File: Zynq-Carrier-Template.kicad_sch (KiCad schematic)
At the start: 17 parts, among them J1 Zynq_SoM, J2 B2B-PH-K-S, J3 USB_C_Receptacle_USB2.0_16P, J4 Conn_01x03, J5 Conn_01x03, U1 BQ25629RYKR, U12 SRV05-4

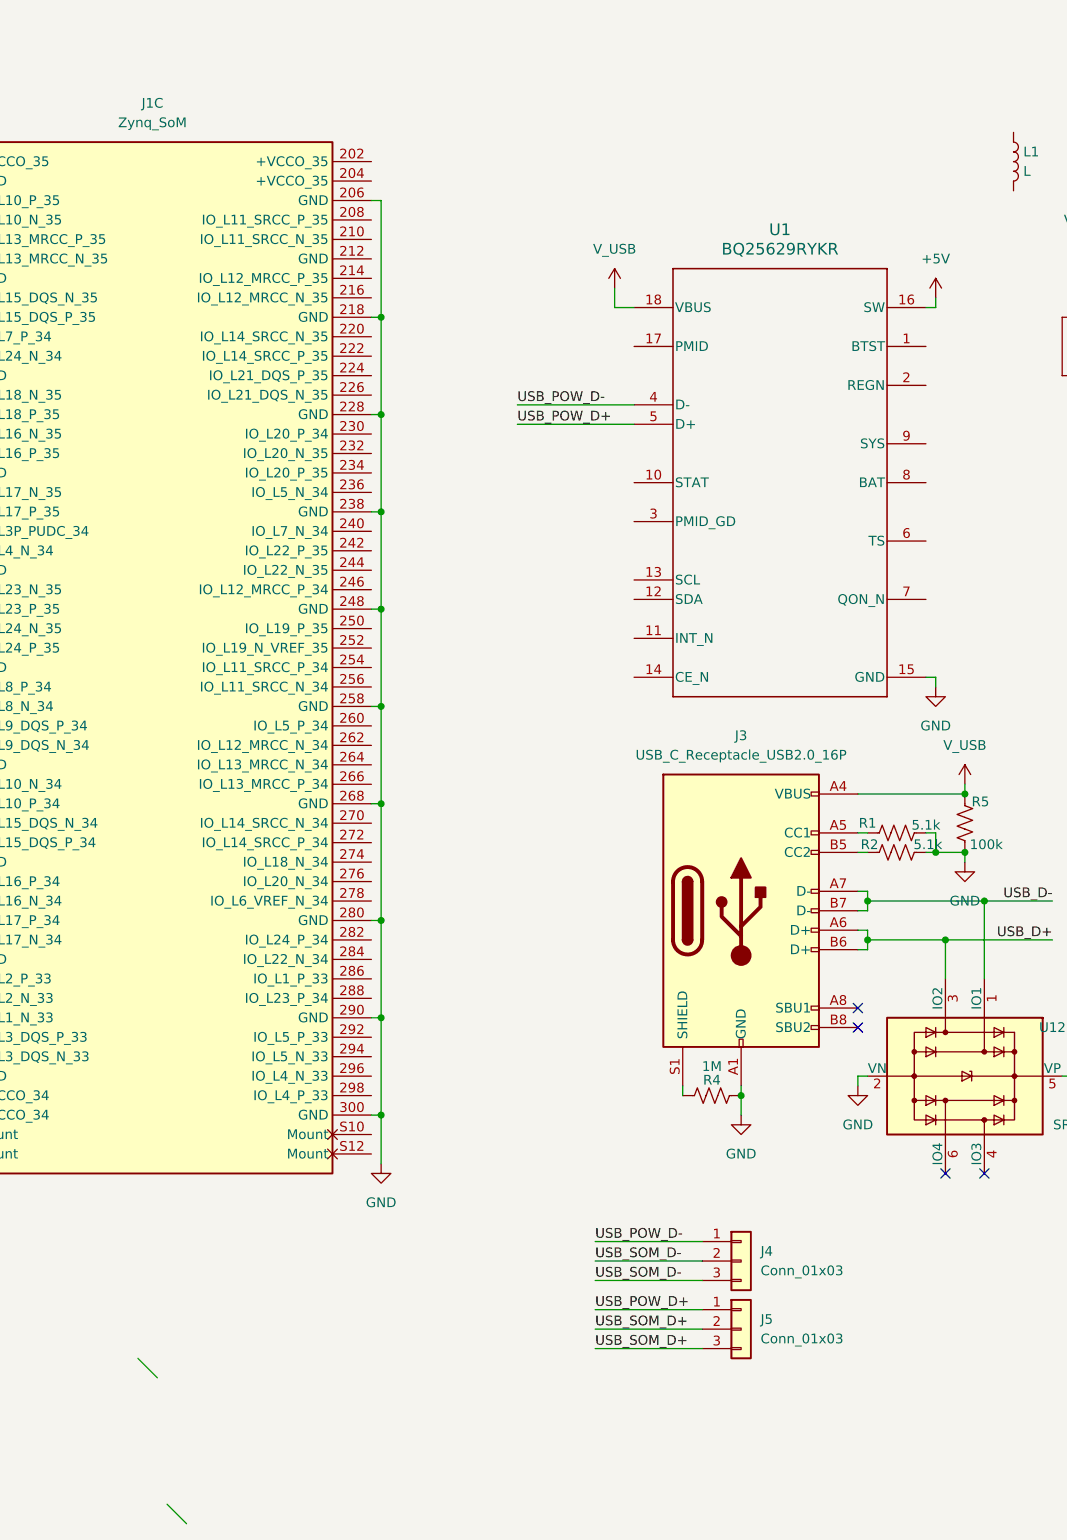
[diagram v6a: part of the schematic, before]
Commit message: Update Zynq-Carrier-Template.kicad_sch
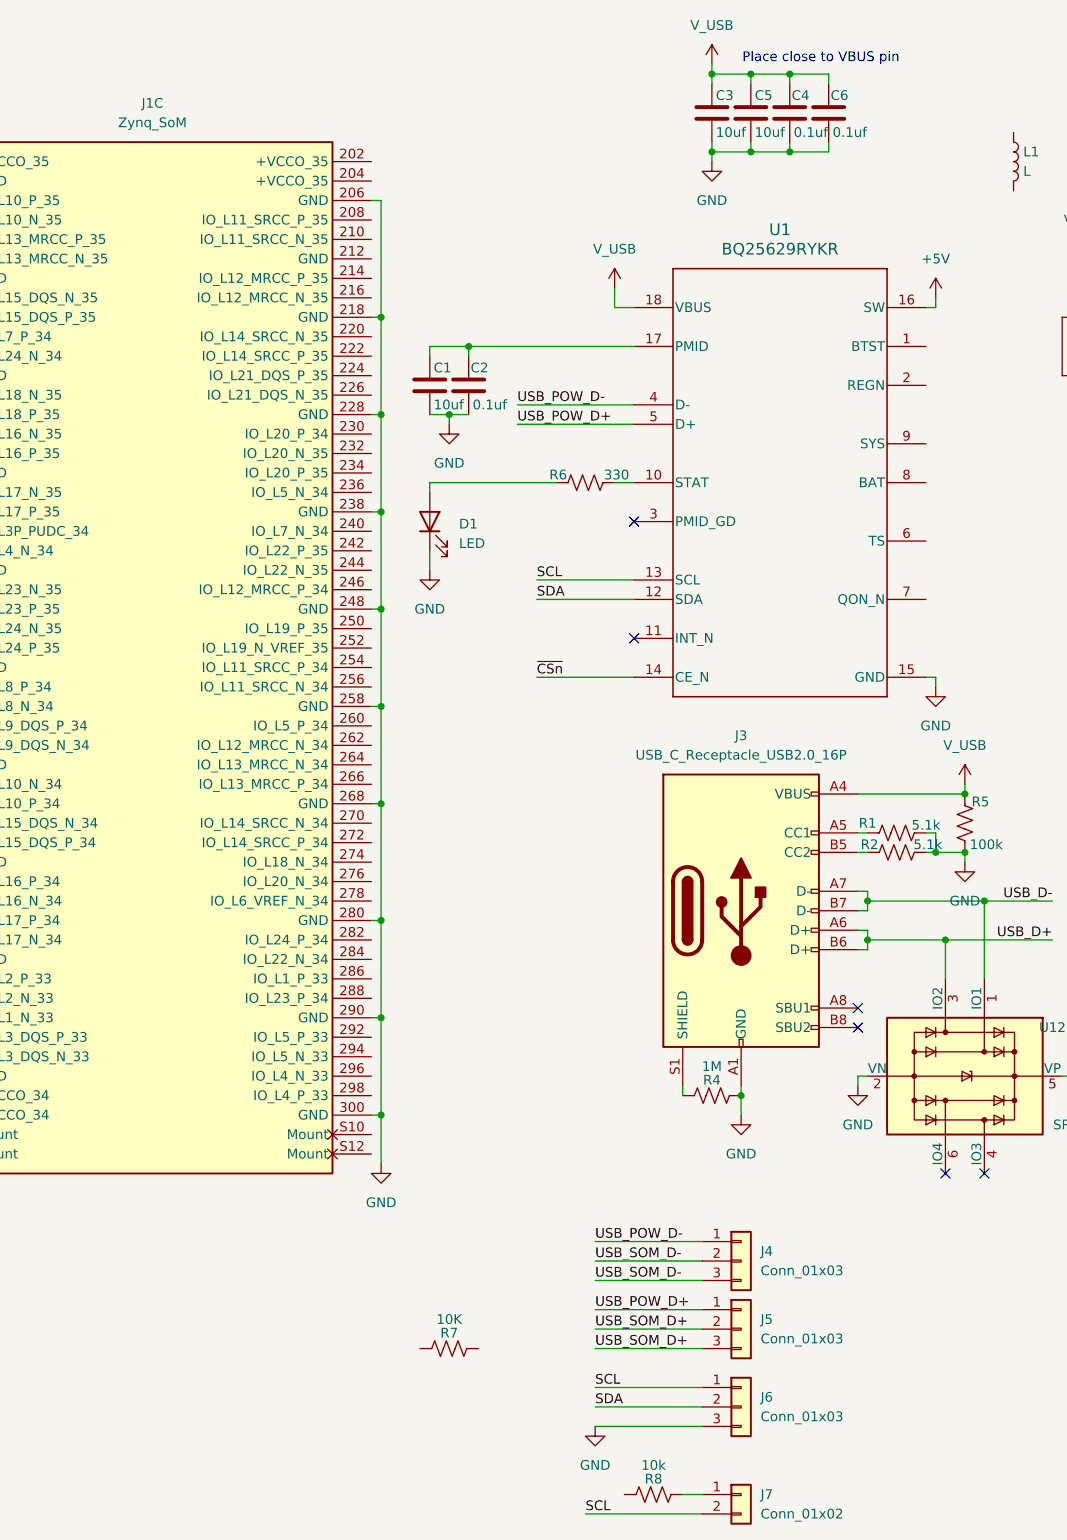
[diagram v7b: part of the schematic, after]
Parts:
- added C1, C3, C5: 10uf, Capacitor_SMD:C_0603_1608Metric, symbol Device:C
- added C2, C4, C6: 0.1uf, Capacitor_SMD:C_0603_1608Metric, symbol Device:C
- added D1: LED, LED_SMD:LED_0805_2012Metric, symbol Device:LED
- added J6: Conn_01x03, Connector_PinHeader_2.54mm:PinHeader_1x03_P2.54mm_Vertical, symbol Connector_Generic:Conn_01x03
- added J7: Conn_01x02, Connector_PinHeader_2.54mm:PinHeader_1x02_P2.54mm_Vertical, symbol Connector_Generic:Conn_01x02
- added R6: 330, Resistor_SMD:R_0603_1608Metric, symbol Device:R_US
- added R7: 10K, Resistor_SMD:R_0603_1608Metric, symbol Device:R_US
- added R8: 10k, Resistor_SMD:R_0603_1608Metric, symbol Device:R_US
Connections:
- net GND: now also C1.2, C2.2, C3.2, C4.2, C5.2, C6.2, D1.1 (K), J6.3 (Pin_3)
- net V_USB: now also C3.1, C4.1, C5.1, C6.1
- net at U1.10 (STAT): now also R6.1
- net SDA: now reaches U1.12 (SDA)
- net SDA: now also J6.2 (Pin_2)
- net SCL: now reaches U1.13 (SCL)
- net SCL: now also J6.1 (Pin_1), J7.2 (Pin_2)
- net ~{CSn}: now reaches U1.14 (CE_N)
- net at U1.17 (PMID): now also C1.1, C2.1
- new net: J7.1 (Pin_1), R8.2
- new net: D1.2 (A), R6.2
- no-connect marks 4 -> 6
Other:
- note added: "Place close to VBUS pin"

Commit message: Updated Schematic Switching Regulator Output
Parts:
- added C7: 4.7 uF, Capacitor_SMD:C_0603_1608Metric, symbol Device:C_Small
- added C8: 47 nF, Capacitor_SMD:C_0603_1608Metric, symbol Device:C_Small
- added J10: Barrel_Jack_MountingPin, Connector_BarrelJack:BarrelJack_Horizontal, symbol Connector:Barrel_Jack_MountingPin
- added J8: Conn_01x02, Connector_PinHeader_2.54mm:PinHeader_1x02_P2.54mm_Vertical, symbol Connector_Generic:Conn_01x02
- added J9: Conn_01x03, Connector_PinHeader_2.54mm:PinHeader_1x03_P2.54mm_Vertical, symbol Connector_Generic:Conn_01x03
- added R10: 10K, Resistor_SMD:R_0603_1608Metric, symbol Device:R_US
- added R11, R9: 4.7k, Resistor_SMD:R_0603_1608Metric, symbol Device:R_US
- J2: footprint CONN2_B2B-PH-K-S_JST -> JST_Pins:CONN2_B2B-PH-K-S_JST
- R8: value 10k -> 4.7k
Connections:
- net +5V: now also R8.1, J9.2 (Pin_2), R11.2, R9.1; no longer U1.16 (SW)
- net GND: now also H1.1, H2.1, H3.1, H4.1, U1.6 (TS), C7.2, J10.2, J10.MP (MountPin)
- net SCL: now also R7.1; no longer J6.1 (Pin_1)
- net SDA: now also J8.2 (Pin_2), R10.1; no longer J6.2 (Pin_2)
- net USB_D+: now also J5.2 (Pin_2)
- net USB_D-: now also J4.2 (Pin_2)
- net USB_SOM_D+: no longer J5.2 (Pin_2)
- net USB_SOM_D-: no longer J4.2 (Pin_2)
- net VBAT: now also U1.8 (BAT)
- net ~{CSn}: now also R11.1
- net at U1.1 (BTST): now also C8.2
- net at U1.2 (REGN): now also C7.1
- net VREG_OUT: now reaches U1.9 (SYS)
- net VREG_OUT: now also L1.2, J9.1 (Pin_1)
- net at L1.1: now also U1.16 (SW), C8.1
- net at R7.2: now also J6.1 (Pin_1)
- new net: J8.1 (Pin_1), R9.2
- new net: J6.2 (Pin_2), R10.2
- new net Vps: J10.1, J9.3 (Pin_3)
- no-connect marks 6 -> 7
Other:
- moved on the sheet: J7, L1, R7, R8
